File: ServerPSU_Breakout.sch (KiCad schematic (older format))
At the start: 4 parts

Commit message: Added New RevC design
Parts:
- removed J_DATA1: 2x5_2.54mm, Connector_PinHeader_2.54mm:PinHeader_2x05_P2.54mm_Horizontal, symbol Connector_Generic:Conn_02x05_Odd_Even
- removed J_GND1, J_VOUT1: 1x6_5.08mm, Samtec HPM-06-02-T-S-RA_1x6:Samtec HPM-06-02-T-S-RA_2x6, symbol Connector_Generic:Conn_01x06
- removed J_PSU_IN1: Amphenol FCI 10046971-001LF, Amphenol FCI 10046971-001LF_2x32:Amphenol_FCI_10046971-001LF_2x32, symbol Connector_Generic:Conn_02x32_Counter_Clockwise
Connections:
- net labels removed: 12V, 12VSB, ADDR, GND, ISHARE, PRESENT, PSINTERRUPT, PSOK, PSON, SCL, SDA
- wire segments 156 -> 22
- no-connect marks 2 -> 1

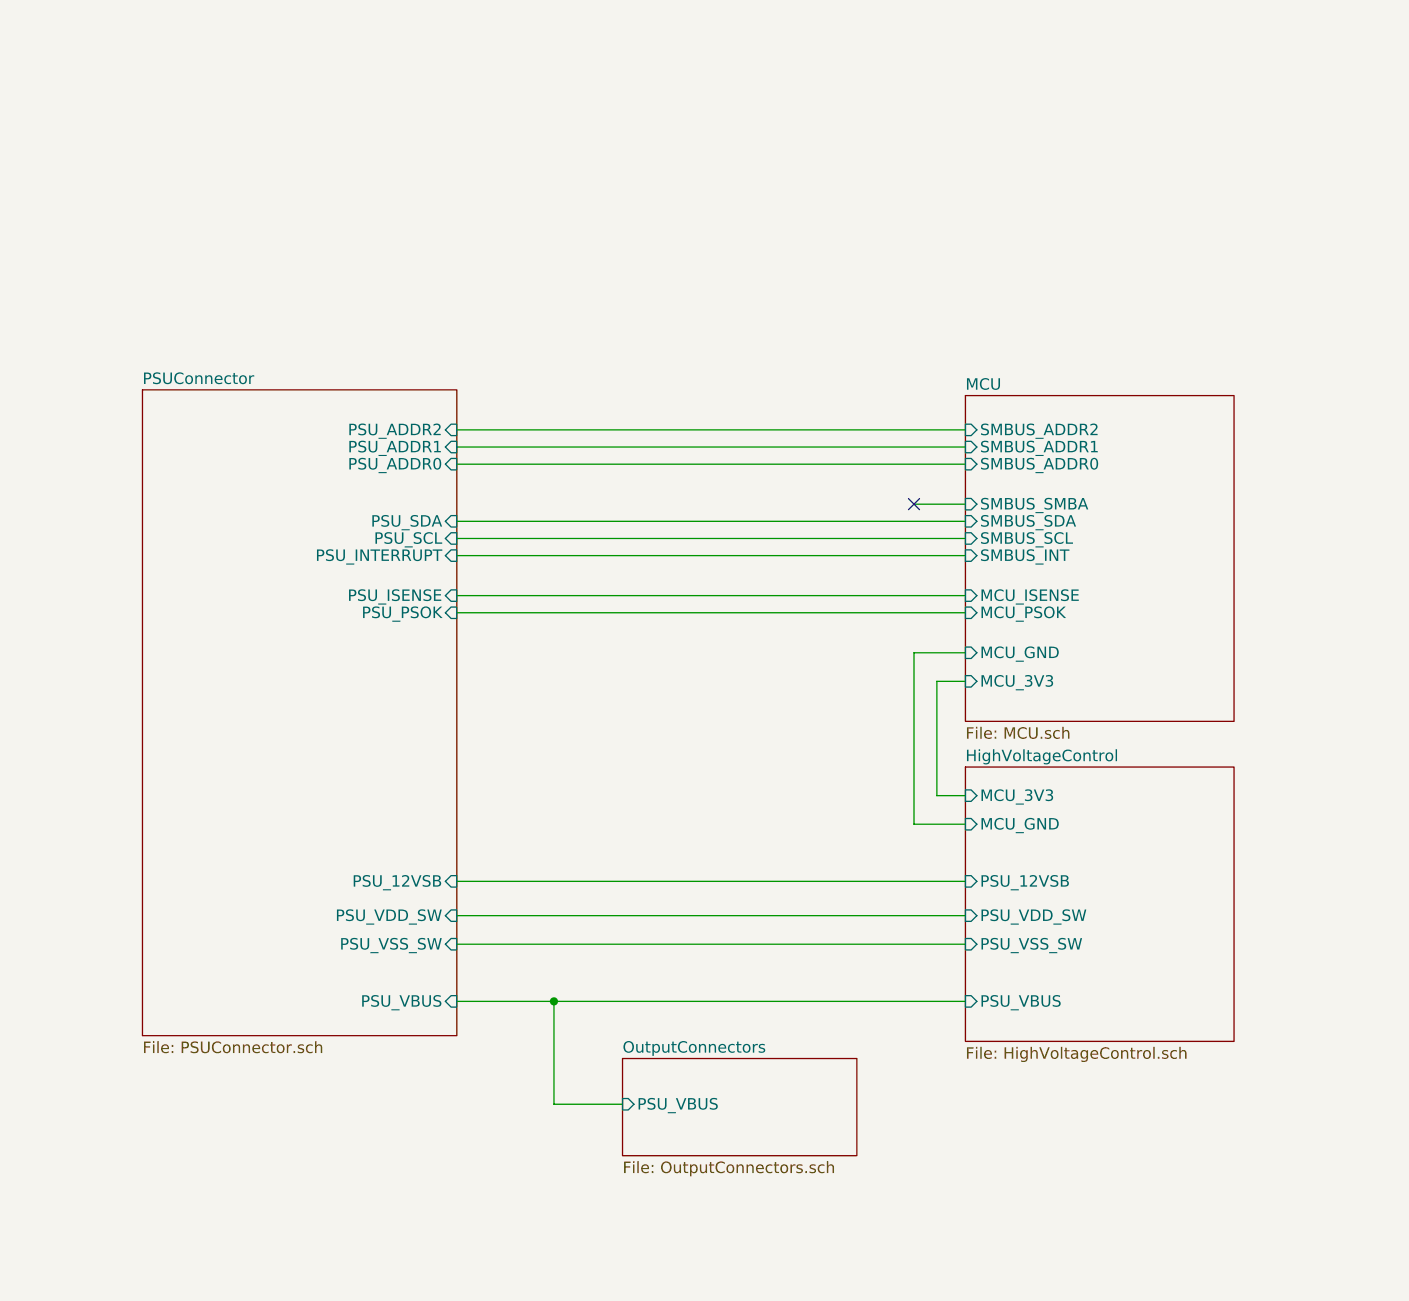
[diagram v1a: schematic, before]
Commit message: UPDATED SWITCH WIRING
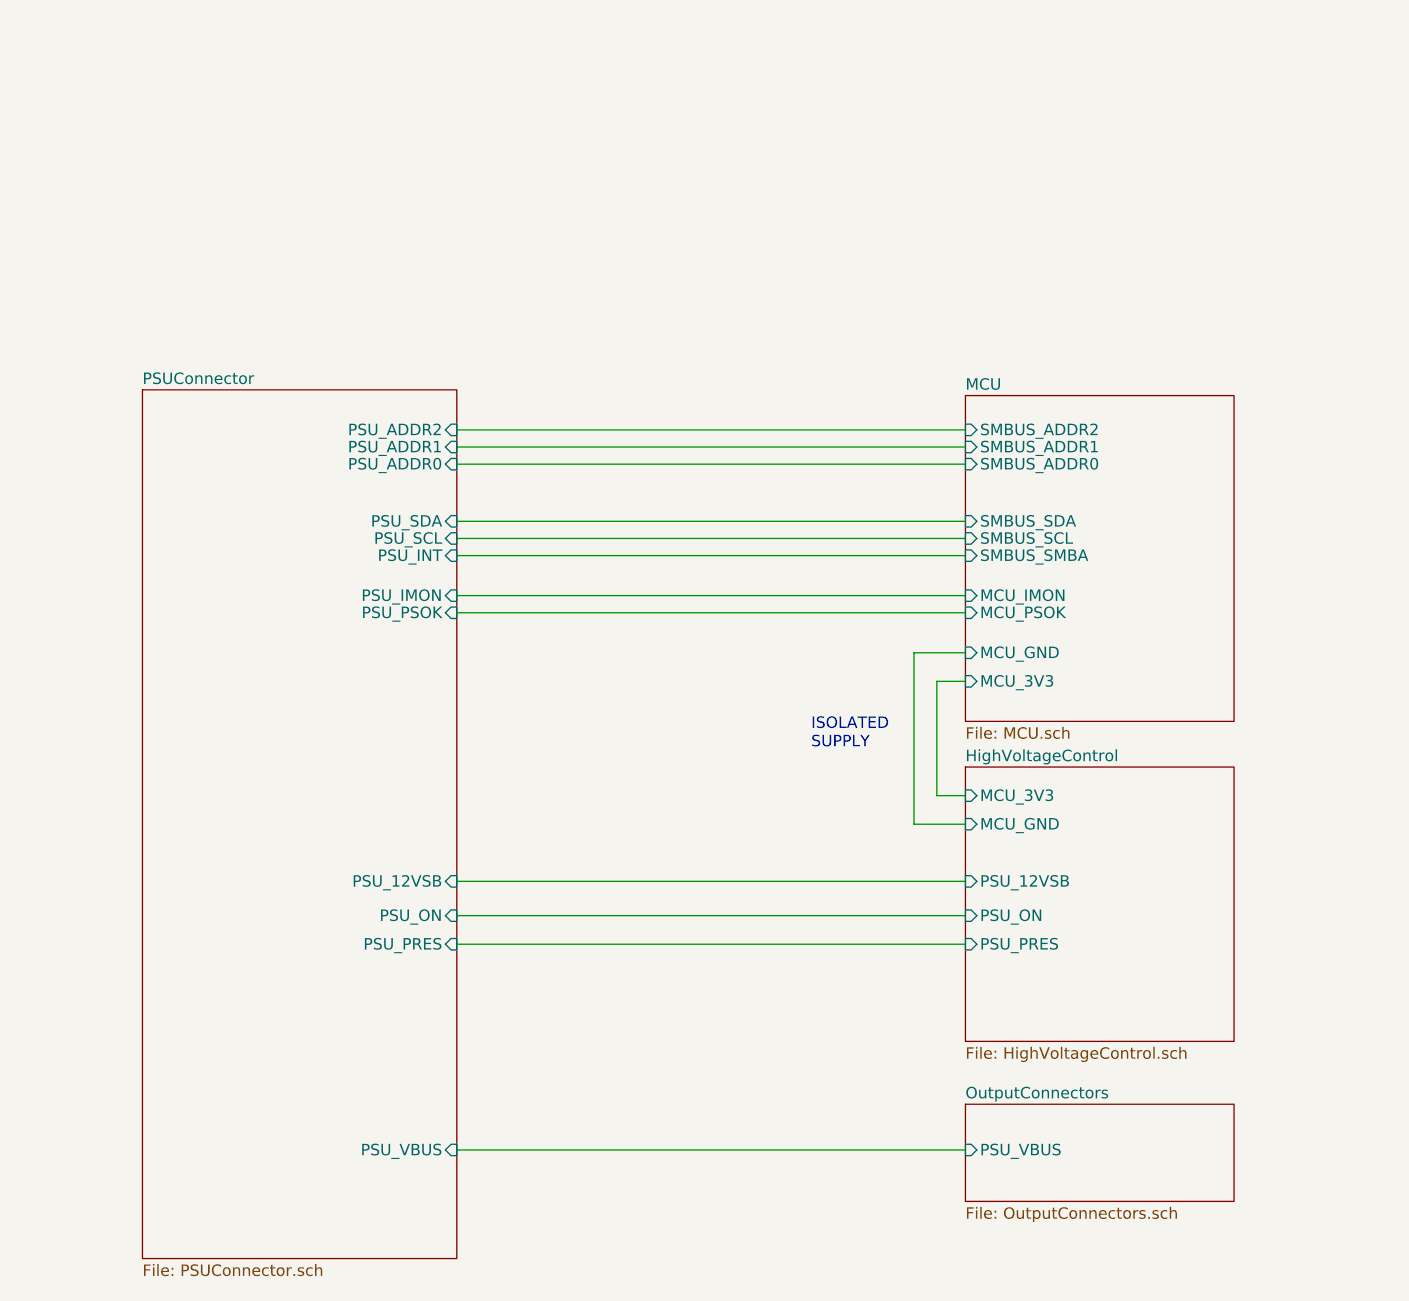
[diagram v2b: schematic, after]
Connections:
- no-connect marks 1 -> 0
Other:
- note added: "ISOLATED\nSUPPLY"
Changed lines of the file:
@@
 $EndDescr
 $Sheet
-S 3750 5900 1025 425
+S 5250 6100 1175 425
 U 5F02DF75
 F0 "OutputConnectors" 50
 F1 "OutputConnectors.sch" 50
-F2 "PSU_VBUS" I L 3750 6100 50
+F2 "PSU_VBUS" I L 5250 6300 50
 $EndSheet
 $Sheet
@@
 F0 "HighVoltageControl" 50
 F1 "HighVoltageControl.sch" 50
-F2 "PSU_VDD_SW" I L 5250 5275 50
-F3 "PSU_VSS_SW" I L 5250 5400 50
-F4 "PSU_12VSB" I L 5250 5125 50
-F5 "PSU_VBUS" I L 5250 5650 50
-F6 "MCU_GND" I L 5250 4875 50
-F7 "MCU_3V3" I L 5250 4750 50
+F2 "PSU_12VSB" I L 5250 5125 50
+F4 "MCU_GND" I L 5250 4875 50
+F5 "MCU_3V3" I L 5250 4750 50
+F6 "PSU_ON" I L 5250 5275 50
+F7 "PSU_PRES" I L 5250 5400 50
 $EndSheet
 $Sheet
@@
 F2 "MCU_GND" I L 5250 4125 50
 F3 "MCU_3V3" I L 5250 4250 50
-F4 "MCU_ISENSE" I L 5250 3875 50
-F5 "MCU_PSOK" I L 5250 3950 50
-F6 "SMBUS_SDA" I L 5250 3550 50
-F7 "SMBUS_SCL" I L 5250 3625 50
-F8 "SMBUS_SMBA" I L 5250 3475 50
-F9 "SMBUS_INT" I L 5250 3700 50
-F10 "SMBUS_ADDR0" I L 5250 3300 50
-F11 "SMBUS_ADDR1" I L 5250 3225 50
-F12 "SMBUS_ADDR2" I L 5250 3150 50
+F4 "MCU_PSOK" I L 5250 3950 50
+F5 "SMBUS_SDA" I L 5250 3550 50
+F6 "SMBUS_SCL" I L 5250 3625 50
+F7 "SMBUS_SMBA" I L 5250 3700 50
+F9 "SMBUS_ADDR0" I L 5250 3300 50
+F10 "SMBUS_ADDR1" I L 5250 3225 50
+F11 "SMBUS_ADDR2" I L 5250 3150 50
+F12 "MCU_IMON" I L 5250 3875 50
 $EndSheet
 Wire Wire Line
@@
 Wire Wire Line
 	3025 5125 5250 5125
-Wire Wire Line
-	5250 5650 3450 5650
 $Sheet
-S 1650 2975 1375 2825
+S 1650 2975 1375 3800
 U 5EFF0F4B
 F0 "PSUConnector" 50
 F1 "PSUConnector.sch" 50
-F2 "PSU_VBUS" I R 3025 5650 50
+F2 "PSU_VBUS" I R 3025 6300 50
 F3 "PSU_ADDR2" I R 3025 3150 50
 F4 "PSU_ADDR1" I R 3025 3225 50
 F5 "PSU_ADDR0" I R 3025 3300 50
 F6 "PSU_12VSB" I R 3025 5125 50
-F7 "PSU_VDD_SW" I R 3025 5275 50
-F8 "PSU_VSS_SW" I R 3025 5400 50
-F9 "PSU_PSOK" I R 3025 3950 50
-F10 "PSU_SDA" I R 3025 3550 50
-F11 "PSU_SCL" I R 3025 3625 50
-F12 "PSU_ISENSE" I R 3025 3875 50
-F13 "PSU_INTERRUPT" I R 3025 3700 50
+F7 "PSU_PSOK" I R 3025 3950 50
+F8 "PSU_SDA" I R 3025 3550 50
+F9 "PSU_SCL" I R 3025 3625 50
+F10 "PSU_ON" I R 3025 5275 50
+F11 "PSU_PRES" I R 3025 5400 50
+F12 "PSU_IMON" I R 3025 3875 50
+F13 "PSU_INT" I R 3025 3700 50
 $EndSheet
 Wire Wire Line
-	3750 6100 3450 6100
-Wire Wire Line
-	3450 6100 3450 5650
-Connection ~ 3450 5650
-Wire Wire Line
-	3450 5650 3025 5650
+	5250 6300 3025 6300
 Wire Wire Line
 	5250 4750 5125 4750
@@
 Wire Wire Line
 	5250 3300 3025 3300
-Wire Wire Line
-	5250 3475 5025 3475
-NoConn ~ 5025 3475
+Text Notes 4575 4550 0    50   ~ 0
+ISOLATED\nSUPPLY
 $EndSCHEMATC

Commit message: layout draft
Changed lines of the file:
@@
 F0 "HighVoltageControl" 50
 F1 "HighVoltageControl.sch" 50
-F2 "PSU_12VSB" I L 5250 5125 50
-F3 "MCU_GND" I L 5250 4875 50
+F2 "PSU_12VSB" I L 5250 5450 50
+F3 "MCU_GND" I L 5250 4850 50
 F4 "MCU_3V3" I L 5250 4750 50
-F5 "PSU_ON" I L 5250 5275 50
-F6 "PSU_PRES" I L 5250 5400 50
+F5 "PSU_ON" I L 5250 5550 50
+F6 "PSU_PRES" I L 5250 5650 50
+F7 "MCU_SW" I L 5250 4950 50
 $EndSheet
+Wire Wire Line
+	5250 5650 3050 5650
+Wire Wire Line
+	3050 5550 5250 5550
+Wire Wire Line
+	3050 5450 5250 5450
+Wire Wire Line
+	5250 6300 3050 6300
+Text Notes 4575 4550 0    50   ~ 0
+ISOLATED\nSUPPLY
+Wire Wire Line
+	5250 3300 3050 3300
+Wire Wire Line
+	5250 3200 3050 3200
+Wire Wire Line
+	5250 3100 3050 3100
 $Sheet
-S 5250 3000 1175 1425
+S 5250 2950 1175 1425
 U 5F02F4E9
 F0 "MCU" 50
 F1 "MCU.sch" 50
-F2 "MCU_GND" I L 5250 4125 50
+F2 "MCU_GND" I L 5250 4150 50
 F3 "MCU_3V3" I L 5250 4250 50
-F4 "MCU_PSOK" I L 5250 3950 50
-F5 "SMBUS_SDA" I L 5250 3550 50
-F6 "SMBUS_SCL" I L 5250 3625 50
-F7 "SMBUS_SMBA" I L 5250 3700 50
+F4 "MCU_PSOK" I L 5250 3900 50
+F5 "SMBUS_SDA" I L 5250 3450 50
+F6 "SMBUS_SCL" I L 5250 3550 50
+F7 "SMBUS_SMBA" I L 5250 3650 50
 F8 "SMBUS_ADDR0" I L 5250 3300 50
-F9 "SMBUS_ADDR1" I L 5250 3225 50
-F10 "SMBUS_ADDR2" I L 5250 3150 50
-F11 "MCU_IMON" I L 5250 3875 50
+F9 "SMBUS_ADDR1" I L 5250 3200 50
+F10 "SMBUS_ADDR2" I L 5250 3100 50
+F11 "MCU_IMON" I L 5250 3800 50
+F12 "MCU_SW" I L 5250 4050 50
 $EndSheet
-Wire Wire Line
-	5250 5400 3025 5400
-Wire Wire Line
-	3025 5275 5250 5275
-Wire Wire Line
-	3025 5125 5250 5125
 $Sheet
-S 1650 2975 1375 3800
+S 1675 2950 1375 3800
 U 5EFF0F4B
 F0 "PSUConnector" 50
 F1 "PSUConnector.sch" 50
-F2 "PSU_VBUS" I R 3025 6300 50
-F3 "PSU_ADDR2" I R 3025 3150 50
-F4 "PSU_ADDR1" I R 3025 3225 50
-F5 "PSU_ADDR0" I R 3025 3300 50
-F6 "PSU_12VSB" I R 3025 5125 50
-F7 "PSU_PSOK" I R 3025 3950 50
-F8 "PSU_SDA" I R 3025 3550 50
-F9 "PSU_SCL" I R 3025 3625 50
-F10 "PSU_ON" I R 3025 5275 50
-F11 "PSU_PRES" I R 3025 5400 50
-F12 "PSU_IMON" I R 3025 3875 50
-F13 "PSU_INT" I R 3025 3700 50
+F2 "PSU_VBUS" I R 3050 6300 50
+F3 "PSU_ADDR2" I R 3050 3100 50
+F4 "PSU_ADDR1" I R 3050 3200 50
+F5 "PSU_ADDR0" I R 3050 3300 50
+F6 "PSU_12VSB" I R 3050 5450 50
+F7 "PSU_PSOK" I R 3050 3900 50
+F8 "PSU_SDA" I R 3050 3450 50
+F9 "PSU_SCL" I R 3050 3550 50
+F10 "PSU_ON" I R 3050 5550 50
+F11 "PSU_PRES" I R 3050 5650 50
+F12 "PSU_IMON" I R 3050 3800 50
+F13 "PSU_INT" I R 3050 3650 50
 $EndSheet
 Wire Wire Line
-	5250 6300 3025 6300
+	3050 3450 5250 3450
 Wire Wire Line
-	5250 4750 5125 4750
+	5250 3550 3050 3550
 Wire Wire Line
-	5125 4250 5250 4250
+	5250 3650 3050 3650
 Wire Wire Line
-	5025 4125 5025 4875
+	5250 3800 3050 3800
 Wire Wire Line
-	5025 4875 5250 4875
+	5250 3900 3050 3900
 Wire Wire Line
-	5025 4125 5250 4125
+	5250 4850 5050 4850
 Wire Wire Line
-	5250 3950 3025 3950
+	5050 4850 5050 4150
 Wire Wire Line
-	5250 3875 3025 3875
+	5050 4150 5250 4150
 Wire Wire Line
-	5125 4750 5125 4250
+	5250 4950 4950 4950
 Wire Wire Line
-	5250 3550 3025 3550
+	4950 4950 4950 4050
 Wire Wire Line
-	3025 3625 5250 3625
+	4950 4050 5250 4050
 Wire Wire Line
-	3025 3700 5250 3700
+	5250 4250 5150 4250
 Wire Wire Line
-	5250 3150 3025 3150
+	5150 4250 5150 4750
 Wire Wire Line
-	3025 3225 5250 3225
-Wire Wire Line
-	5250 3300 3025 3300
-Text Notes 4575 4550 0    50   ~ 0
-ISOLATED\nSUPPLY
+	5150 4750 5250 4750
 $EndSCHEMATC

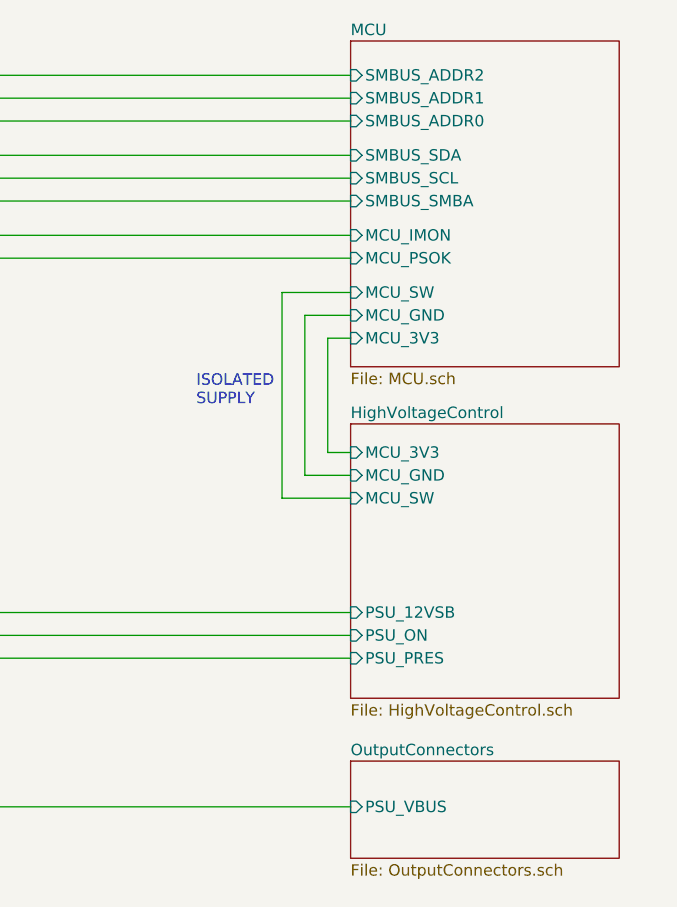
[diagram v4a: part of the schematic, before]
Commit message: Added TFT Delayed Reset sub circuit
changed NCS1S1203SC to NCS1S1205SC
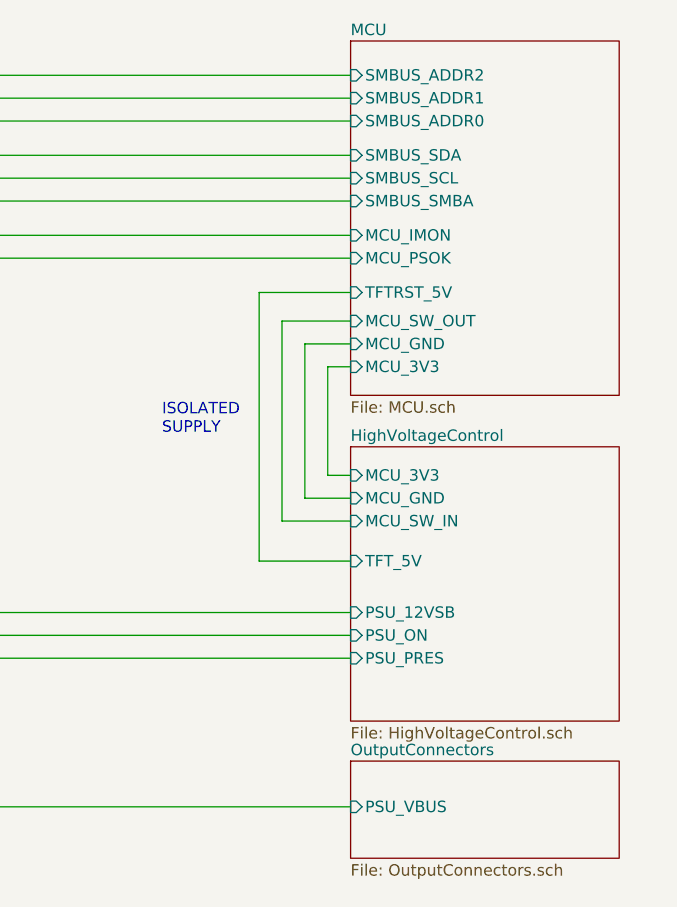
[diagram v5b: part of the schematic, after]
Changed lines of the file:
@@
 $Descr A4 8268 11693 portrait
 encoding utf-8
-Sheet 1 5
+Sheet 1 6
 Title ""
 Date "2020-06-30"
@@
 F2 "PSU_VBUS" I L 5250 6300 50
 $EndSheet
-$Sheet
-S 5250 4625 1175 1200
-U 5F02F4C5
-F0 "HighVoltageControl" 50
-F1 "HighVoltageControl.sch" 50
-F2 "PSU_12VSB" I L 5250 5450 50
-F3 "MCU_GND" I L 5250 4850 50
-F4 "MCU_3V3" I L 5250 4750 50
-F5 "PSU_ON" I L 5250 5550 50
-F6 "PSU_PRES" I L 5250 5650 50
-F7 "MCU_SW" I L 5250 4950 50
-$EndSheet
 Wire Wire Line
 	5250 5650 3050 5650
@@
 Wire Wire Line
 	5250 6300 3050 6300
-Text Notes 4575 4550 0    50   ~ 0
+Text Notes 4425 4675 0    50   ~ 0
 ISOLATED\nSUPPLY
 Wire Wire Line
@@
 	5250 3100 3050 3100
 $Sheet
-S 5250 2950 1175 1425
+S 5250 2950 1175 1550
 U 5F02F4E9
 F0 "MCU" 50
 F1 "MCU.sch" 50
-F2 "MCU_GND" I L 5250 4150 50
-F3 "MCU_3V3" I L 5250 4250 50
+F2 "MCU_GND" I L 5250 4275 50
+F3 "MCU_3V3" I L 5250 4375 50
 F4 "MCU_PSOK" I L 5250 3900 50
 F5 "SMBUS_SDA" I L 5250 3450 50
@@
 F10 "SMBUS_ADDR2" I L 5250 3100 50
 F11 "MCU_IMON" I L 5250 3800 50
-F12 "MCU_SW" I L 5250 4050 50
+F12 "TFTRST_5V" I L 5250 4050 50
+F13 "MCU_SW_OUT" I L 5250 4175 50
 $EndSheet
 $Sheet
@@
 	5250 3900 3050 3900
 Wire Wire Line
-	5250 4850 5050 4850
+	5050 4275 5250 4275
 Wire Wire Line
-	5050 4850 5050 4150
+	4950 4175 5250 4175
 Wire Wire Line
-	5050 4150 5250 4150
+	5250 4375 5150 4375
 Wire Wire Line
-	5250 4950 4950 4950
+	5150 4375 5150 4850
 Wire Wire Line
-	4950 4950 4950 4050
+	5150 4850 5250 4850
 Wire Wire Line
-	4950 4050 5250 4050
+	5050 4950 5050 4275
 Wire Wire Line
-	5250 4250 5150 4250
+	5250 4950 5050 4950
 Wire Wire Line
-	5150 4250 5150 4750
+	4950 5050 4950 4175
 Wire Wire Line
-	5150 4750 5250 4750
+	5250 5050 4950 5050
+$Sheet
+S 5250 4725 1175 1200
+U 5F02F4C5
+F0 "HighVoltageControl" 50
+F1 "HighVoltageControl.sch" 50
+F2 "PSU_12VSB" I L 5250 5450 50
+F3 "MCU_GND" I L 5250 4950 50
+F4 "MCU_3V3" I L 5250 4850 50
+F5 "PSU_ON" I L 5250 5550 50
+F6 "PSU_PRES" I L 5250 5650 50
+F7 "MCU_SW_IN" I L 5250 5050 50
+F8 "TFT_5V" I L 5250 5225 50
+$EndSheet
+Wire Wire Line
+	5250 4050 4850 4050
+Wire Wire Line
+	4850 4050 4850 5225
+Wire Wire Line
+	4850 5225 5250 5225
 $EndSCHEMATC
